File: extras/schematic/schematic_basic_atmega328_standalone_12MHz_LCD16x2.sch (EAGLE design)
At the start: 27 parts, among them U1 SI4735-D60-GU, U2 328P, Y2 12MHz

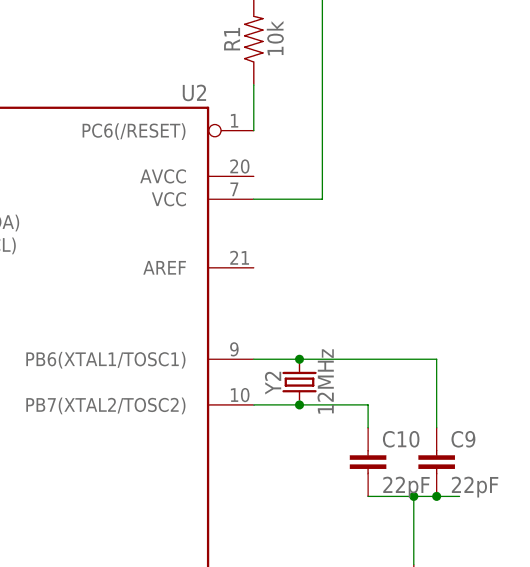
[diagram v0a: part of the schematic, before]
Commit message: SI473X Arduino Library
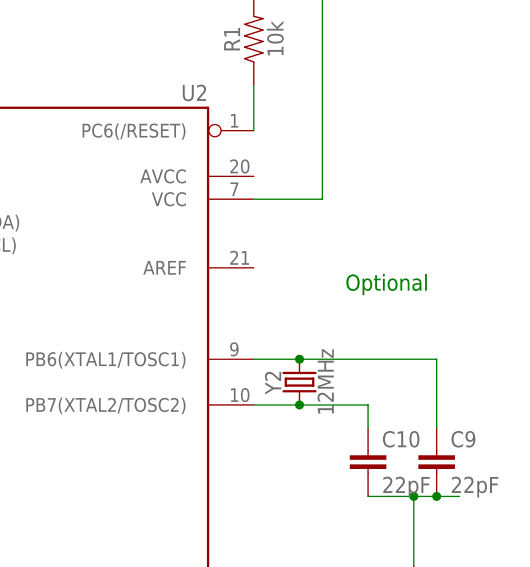
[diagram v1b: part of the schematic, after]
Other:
- note added: "Optional"
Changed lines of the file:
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@@
 <text x="63.5" y="124.46" size="1.778" layer="91">D2</text>
 <text x="71.12" y="109.22" size="1.778" layer="91">D3</text>
+<text x="162.56" y="124.46" size="1.778" layer="91">Optional </text>
+<rectangle x1="149.86" y1="99.06" x2="182.88" y2="121.92" layer="207"/>
 </plain>
 <instances>
